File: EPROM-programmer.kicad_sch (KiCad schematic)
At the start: 83 parts, among them J1 ZIF-socket, J10 AMP_VPP, J2 ISP, J3 DAC_VCC, J4 DAC_VPP, J5 GND, J6 Barrel_Jack_Switch, J7 ZIF_VCC, J8 AMP_VCC, J9 GND, P1 USB-C, Q1 BC327, Q2 BC327, Q3 BC327, Q4 BC327, Q5 BC327, Q6 BC327, SW1 SW_Push, U1 ATmega1284-P, U2 MCP2221AxP, U3 MCP4812, U4 LM358, U5 ULN2003, U6 LM317_TO-220, U7 LM317_TO-220, Y1 20M

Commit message: Route VPP-stuff
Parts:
- removed R11, R21, R23: 5.1K, Resistor_THT:R_Axial_DIN0207_L6.3mm_D2.5mm_P10.16mm_Horizontal, symbol Device:R
- added RN1: 4K7, Resistor_THT:R_Array_SIP4, symbol Device:R_Network03_Split
- R12, R15, R22, R24: value 5.1K -> 5K1
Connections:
- net AMP_VPP: now also RN1.1 (R1), RN1.1 (R1), RN1.1 (R1)
- net at Q5.2 (B), R22.1: now also RN1.3 (R2.2)
- net at Q4.2 (B), R12.1: now also RN1.4 (R3.2)
- net at Q6.2 (B), R24.1: now also RN1.2 (R1.2)
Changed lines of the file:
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@@
 	)
 	(symbol
+		(lib_id "Device:R_Network03_Split")
+		(at 260.35 33.02 90)
+		(unit 3)
+		(exclude_from_sim no)
+		(in_bom yes)
+		(on_board yes)
+		(dnp no)
+		(fields_autoplaced yes)
+		(property "Reference" "RN1"
+			(at 260.35 26.67 90)
+			(effects
+				(font
+					(size 1.27 1.27)
+				)
+			)
+		)
+		(property "Value" "4K7"
+			(at 260.35 29.21 90)
+			(effects
+				(font
+					(size 1.27 1.27)
+				)
+			)
+		)
+		(property "Footprint" "Resistor_THT:R_Array_SIP4"
+			(at 260.35 35.052 90)
+			(effects
+				(font
+					(size 1.27 1.27)
+				)
+				(hide yes)
+			)
+		)
+		(property "Datasheet" "http://www.vishay.com/docs/31509/csc.pdf"
+			(at 260.35 33.02 0)
+			(effects
+				(font
+					(size 1.27 1.27)
+				)
+				(hide yes)
+			)
+		)
+		(property "Description" "3 resistor network, star topology, bussed resistors, split"
+			(at 260.35 33.02 0)
+			(effects
+				(font
+					(size 1.27 1.27)
+				)
+				(hide yes)
+			)
+		)
+		(pin "1"
+		)
+		(pin "3"
+		)
+		(pin "4"
+		)
+		(pin "2"
+		)
+		(instances
+			(project "EPROM-programmer"
+				(path "/8c5576b1-cb3e-4456-837b-2f47818a03ab"
+					(reference "RN1")
+					(unit 3)
+				)
+			)
+		)
+	)
+	(symbol
 		(lib_id "Device:C")
 		(at 92.71 161.29 0)
@@
 	)
 	(symbol
+		(lib_id "Device:R_Network03_Split")
+		(at 260.35 62.23 90)
+		(unit 2)
+		(exclude_from_sim no)
+		(in_bom yes)
+		(on_board yes)
+		(dnp no)
+		(fields_autoplaced yes)
+		(property "Reference" "RN1"
+			(at 260.35 55.88 90)
+			(effects
+				(font
+					(size 1.27 1.27)
+				)
+			)
+		)
+		(property "Value" "4K7"
+			(at 260.35 58.42 90)
+			(effects
+				(font
+					(size 1.27 1.27)
+				)
+			)
+		)
+		(property "Footprint" "Resistor_THT:R_Array_SIP4"
+			(at 260.35 64.262 90)
+			(effects
+				(font
+					(size 1.27 1.27)
+				)
+				(hide yes)
+			)
+		)
+		(property "Datasheet" "http://www.vishay.com/docs/31509/csc.pdf"
+			(at 260.35 62.23 0)
+			(effects
+				(font
+					(size 1.27 1.27)
+				)
+				(hide yes)
+			)
+		)
+		(property "Description" "3 resistor network, star topology, bussed resistors, split"
+			(at 260.35 62.23 0)
+			(effects
+				(font
+					(size 1.27 1.27)
+				)
+				(hide yes)
+			)
+		)
+		(pin "1"
+		)
+		(pin "3"
+		)
+		(pin "4"
+		)
+		(pin "2"
+		)
+		(instances
+			(project ""
+				(path "/8c5576b1-cb3e-4456-837b-2f47818a03ab"
+					(reference "RN1")
+					(unit 2)
+				)
+			)
+		)
+	)
+	(symbol
 		(lib_id "Device:R")
 		(at 259.08 129.54 0)
@@
 			)
 		)
-		(property "Value" "5.1K"
+		(property "Value" "5K1"
 			(at 270.51 71.12 0)
 			(effects
@@
 			)
 		)
-		(property "Value" "5.1K"
+		(property "Value" "5K1"
 			(at 270.51 100.33 0)
 			(effects
@@
 	)
 	(symbol
-		(lib_id "Device:R")
-		(at 260.35 91.44 90)
-		(unit 1)
-		(exclude_from_sim no)
-		(in_bom yes)
-		(on_board yes)
-		(dnp no)
-		(property "Reference" "R23"
-			(at 261.62 88.9 90)
-			(effects
-				(font
-					(size 1.27 1.27)
-				)
-				(justify left)
-			)
-		)
-		(property "Value" "5.1K"
-			(at 261.62 86.36 90)
-			(effects
-				(font
-					(size 1.27 1.27)
-				)
-				(justify left)
-			)
-		)
-		(property "Footprint" "Resistor_THT:R_Axial_DIN0207_L6.3mm_D2.5mm_P10.16mm_Horizontal"
-			(at 260.35 93.218 90)
-			(effects
-				(font
-					(size 1.27 1.27)
-				)
-				(hide yes)
-			)
-		)
-		(property "Datasheet" "~"
-			(at 260.35 91.44 0)
-			(effects
-				(font
-					(size 1.27 1.27)
-				)
-				(hide yes)
-			)
-		)
-		(property "Description" ""
-			(at 260.35 91.44 0)
-			(effects
-				(font
-					(size 1.27 1.27)
-				)
-				(hide yes)
-			)
-		)
-		(pin "1"
-		)
-		(pin "2"
-		)
-		(instances
-			(project "EPROM-programmer"
-				(path "/8c5576b1-cb3e-4456-837b-2f47818a03ab"
-					(reference "R23")
-					(unit 1)
-				)
-			)
-		)
-	)
-	(symbol
 		(lib_name "GND_1")
 		(lib_id "power:GND")
@@
 			)
 		)
-		(property "Value" "5.1K"
+		(property "Value" "5K1"
 			(at 171.45 49.53 0)
 			(effects
@@
 	)
 	(symbol
-		(lib_id "Device:R")
-		(at 260.35 33.02 90)
-		(unit 1)
-		(exclude_from_sim no)
-		(in_bom yes)
-		(on_board yes)
-		(dnp no)
-		(property "Reference" "R11"
-			(at 261.62 30.48 90)
-			(effects
-				(font
-					(size 1.27 1.27)
-				)
-				(justify left)
-			)
-		)
-		(property "Value" "5.1K"
-			(at 261.62 27.94 90)
-			(effects
-				(font
-					(size 1.27 1.27)
-				)
-				(justify left)
-			)
-		)
-		(property "Footprint" "Resistor_THT:R_Axial_DIN0207_L6.3mm_D2.5mm_P10.16mm_Horizontal"
-			(at 260.35 34.798 90)
-			(effects
-				(font
-					(size 1.27 1.27)
-				)
-				(hide yes)
-			)
-		)
-		(property "Datasheet" "~"
-			(at 260.35 33.02 0)
-			(effects
-				(font
-					(size 1.27 1.27)
-				)
-				(hide yes)
-			)
-		)
-		(property "Description" ""
-			(at 260.35 33.02 0)
-			(effects
-				(font
-					(size 1.27 1.27)
-				)
-				(hide yes)
-			)
-		)
-		(pin "1"
-		)
-		(pin "2"
-		)
-		(instances
-			(project "EPROM-programmer"
-				(path "/8c5576b1-cb3e-4456-837b-2f47818a03ab"
-					(reference "R11")
-					(unit 1)
-				)
-			)
-		)
-	)
-	(symbol
 		(lib_name "GND_1")
 		(lib_id "power:GND")
@@
 			)
 		)
-		(property "Value" "5.1K"
+		(property "Value" "5K1"
 			(at 270.51 41.91 0)
 			(effects
@@
 	)
 	(symbol
-		(lib_id "Device:R")
-		(at 260.35 62.23 90)
-		(unit 1)
-		(exclude_from_sim no)
-		(in_bom yes)
-		(on_board yes)
-		(dnp no)
-		(property "Reference" "R21"
-			(at 261.62 59.69 90)
-			(effects
-				(font
-					(size 1.27 1.27)
-				)
-				(justify left)
-			)
-		)
-		(property "Value" "5.1K"
-			(at 261.62 57.15 90)
-			(effects
-				(font
-					(size 1.27 1.27)
-				)
-				(justify left)
-			)
-		)
-		(property "Footprint" "Resistor_THT:R_Axial_DIN0207_L6.3mm_D2.5mm_P10.16mm_Horizontal"
-			(at 260.35 64.008 90)
-			(effects
-				(font
-					(size 1.27 1.27)
-				)
-				(hide yes)
-			)
-		)
-		(property "Datasheet" "~"
-			(at 260.35 62.23 0)
-			(effects
-				(font
-					(size 1.27 1.27)
-				)
-				(hide yes)
-			)
-		)
-		(property "Description" ""
-			(at 260.35 62.23 0)
-			(effects
-				(font
-					(size 1.27 1.27)
-				)
-				(hide yes)
-			)
-		)
-		(pin "1"
-		)
-		(pin "2"
-		)
-		(instances
-			(project "EPROM-programmer"
-				(path "/8c5576b1-cb3e-4456-837b-2f47818a03ab"
-					(reference "R21")
-					(unit 1)
-				)
-			)
-		)
-	)
-	(symbol
 		(lib_name "GND_1")
 		(lib_id "power:GND")
@@
 					(unit 1)
 				)
+			)
+		)
+	)
+	(symbol
+		(lib_id "Device:R_Network03_Split")
+		(at 260.35 91.44 90)
+		(unit 1)
+		(exclude_from_sim no)
+		(in_bom yes)
+		(on_board yes)
+		(dnp no)
+		(fields_autoplaced yes)
+		(property "Reference" "RN1"
+			(at 260.35 85.09 90)
+			(effects
+				(font
+					(size 1.27 1.27)
+				)
+			)
+		)
+		(property "Value" "4K7"
+			(at 260.35 87.63 90)
+			(effects
+				(font
+					(size 1.27 1.27)
+				)
+			)
+		)
+		(property "Footprint" "Resistor_THT:R_Array_SIP4"
+			(at 260.35 93.472 90)
+			(effects
+				(font
+					(size 1.27 1.27)
+				)
+				(hide yes)
+			)
+		)
+		(property "Datasheet" "http://www.vishay.com/docs/31509/csc.pdf"
+			(at 260.35 91.44 0)
+			(effects
+				(font
+					(size 1.27 1.27)
+				)
+				(hide yes)
+			)
+		)
+		(property "Description" "3 resistor network, star topology, bussed resistors, split"
+			(at 260.35 91.44 0)
+			(effects
+				(font
+					(size 1.27 1.27)
+				)
+				(hide yes)
+			)
+		)
+		(pin "1"
+		)
+		(pin "3"
+		)
+		(pin "4"
+		)
+		(pin "2"
+		)
+		(instances
+			(project "EPROM-programmer"
+				(path "/8c5576b1-cb3e-4456-837b-2f47818a03ab"
+					(reference "RN1")
+					(unit 1)
+				)

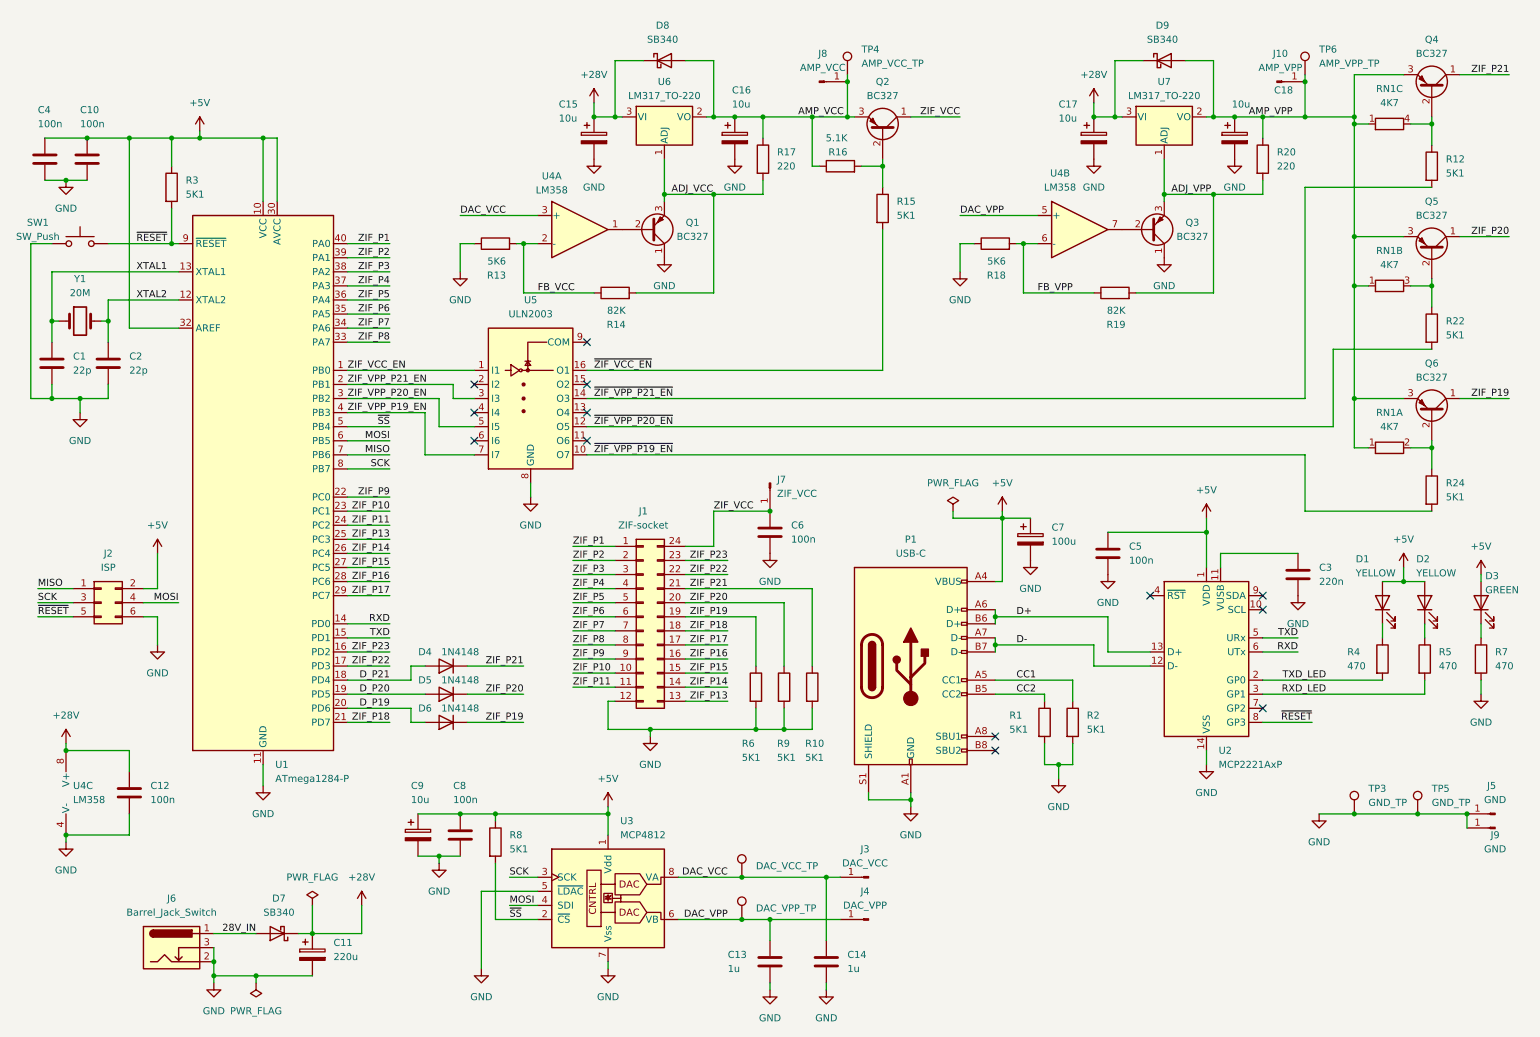
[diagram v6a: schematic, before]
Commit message: Add switching supply for VCC to ZIF-socket
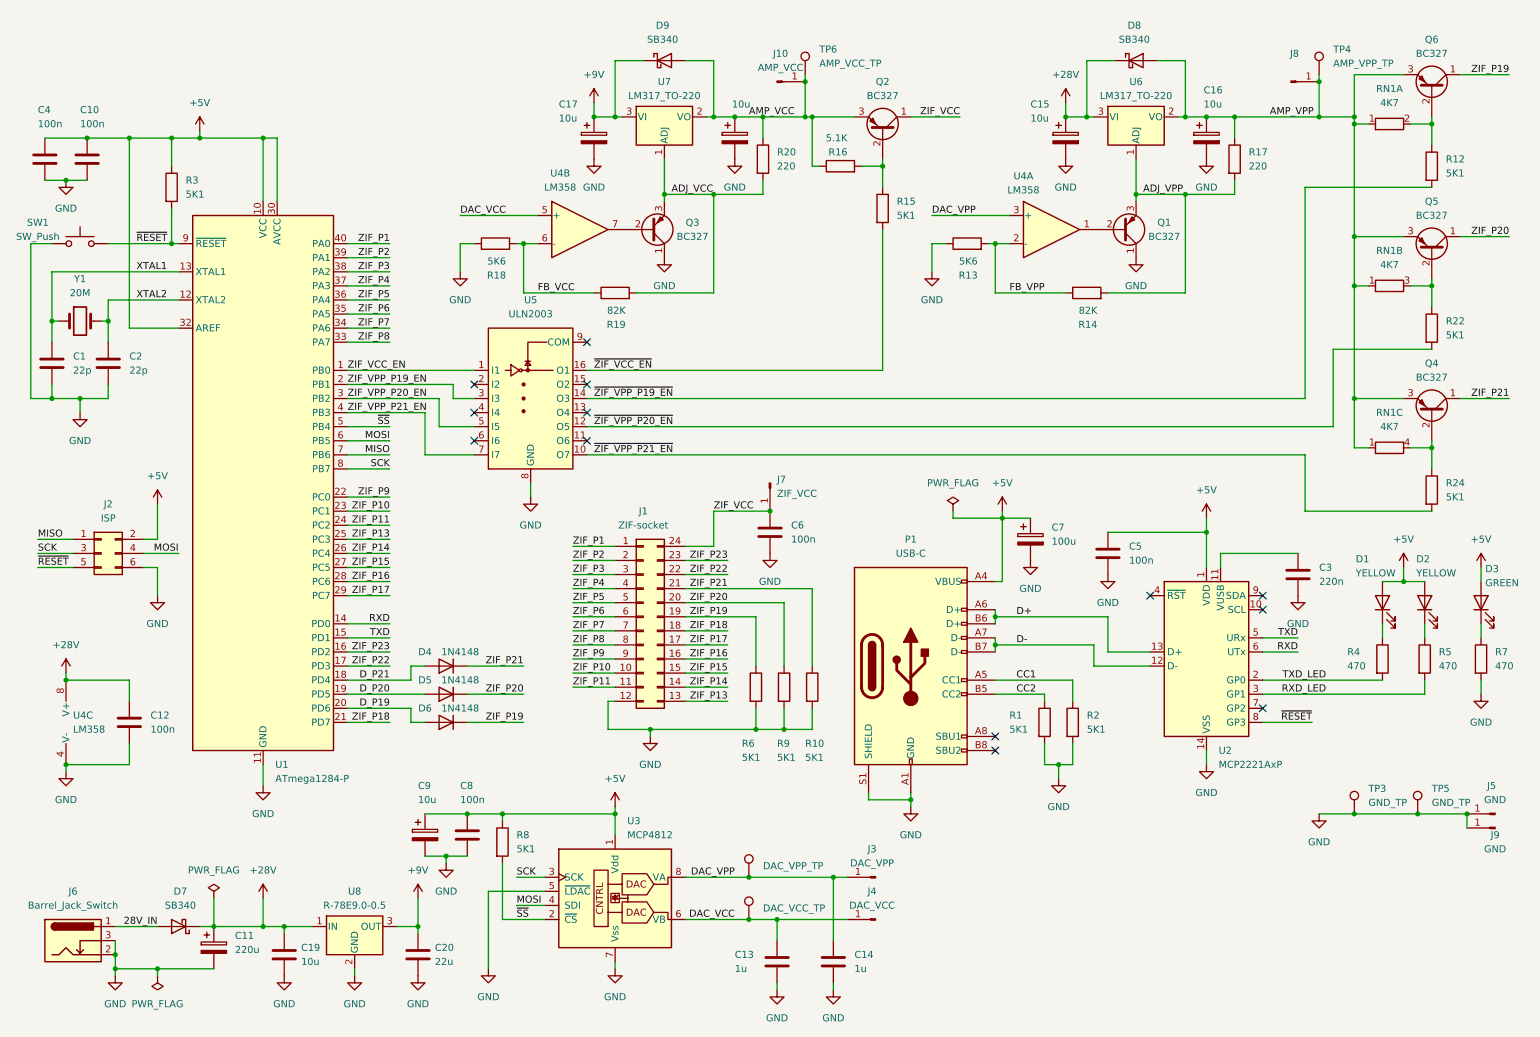
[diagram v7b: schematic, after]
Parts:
- added C19: 10u, Capacitor_THT:C_Rect_L7.0mm_W4.5mm_P5.00mm, symbol Device:C
- added C20: 22u, Capacitor_THT:C_Rect_L7.0mm_W4.5mm_P5.00mm, symbol Device:C
- added U8: R-78E9.0-0.5, Converter_DCDC:Converter_DCDC_RECOM_R-78E-0.5_THT, symbol Regulator_Switching:R-78E9.0-0.5
- J10: value AMP_VPP -> AMP_VCC
- J3: value DAC_VCC -> DAC_VPP
- J4: value DAC_VPP -> DAC_VCC
- J8: value AMP_VCC -> AMP_VPP
- TP1: value DAC_VCC_TP -> DAC_VPP_TP
- TP2: value DAC_VPP_TP -> DAC_VCC_TP
- TP4: value AMP_VCC_TP -> AMP_VPP_TP
- TP6: value AMP_VPP_TP -> AMP_VCC_TP
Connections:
- net +28V: now also C19.1, U8.1 (IN); no longer C17.1, D9.1 (K), U7.3 (VI)
- net ADJ_VCC: now also Q3.3 (E), R19.2, R20.2, U7.1 (ADJ); no longer Q1.3 (E), R14.2, R17.2, U6.1 (ADJ)
- net ADJ_VPP: now also Q1.3 (E), R14.2, R17.2, U6.1 (ADJ); no longer Q3.3 (E), R19.2, R20.2, U7.1 (ADJ)
- net AMP_VCC: now also C18.1, D9.2 (A), J10.1 (Pin_1), R20.1, TP6.1, U7.2 (VO); no longer C16.1, D8.2 (A), J8.1 (Pin_1), R17.1, TP4.1, U6.2 (VO)
- net AMP_VPP: now also C16.1, D8.2 (A), J8.1 (Pin_1), R17.1, TP4.1, U6.2 (VO); no longer C18.1, D9.2 (A), J10.1 (Pin_1), R20.1, TP6.1, U7.2 (VO)
- net DAC_VCC: now also C13.1, J4.1 (Pin_1), TP2.1, U3.6 (VB), U4.5 (+); no longer C14.1, J3.1 (Pin_1), TP1.1, U3.8 (VA), U4.3 (+)
- net DAC_VPP: now also C14.1, J3.1 (Pin_1), TP1.1, U3.8 (VA), U4.3 (+); no longer C13.1, J4.1 (Pin_1), TP2.1, U3.6 (VB), U4.5 (+)
- net FB_VCC: now also R18.2, R19.1, U4.6 (-); no longer R13.2, R14.1, U4.2 (-)
- net FB_VPP: now also R13.2, R14.1, U4.2 (-); no longer R18.2, R19.1, U4.6 (-)
- net GND: now also C19.2, C20.2, U8.2 (GND)
- net ZIF_VPP_P19_EN: now also U1.2 (PB1), U5.3 (I3); no longer U1.4 (PB3), U5.7 (I7)
- net ZIF_VPP_P21_EN: now also U1.4 (PB3), U5.7 (I7); no longer U1.2 (PB1), U5.3 (I3)
- net ~{ZIF_VPP_P19_EN}: now also R12.2, U5.14 (O3); no longer R24.2, U5.10 (O7)
- net ~{ZIF_VPP_P21_EN}: now also R24.2, U5.10 (O7); no longer R12.2, U5.14 (O3)
- net at Q4.2 (B), RN1.4 (R3.2): now also R24.1; no longer R12.1
- net at Q6.2 (B), RN1.2 (R1.2): now also R12.1; no longer R24.1
- new net +9V: C17.1, C20.1, D9.1 (K), U7.3 (VI), U8.3 (OUT)
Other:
- moved on the sheet: C11, C12, C13, C14, C15, C16, C17, C8, C9, D7, D8, D9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

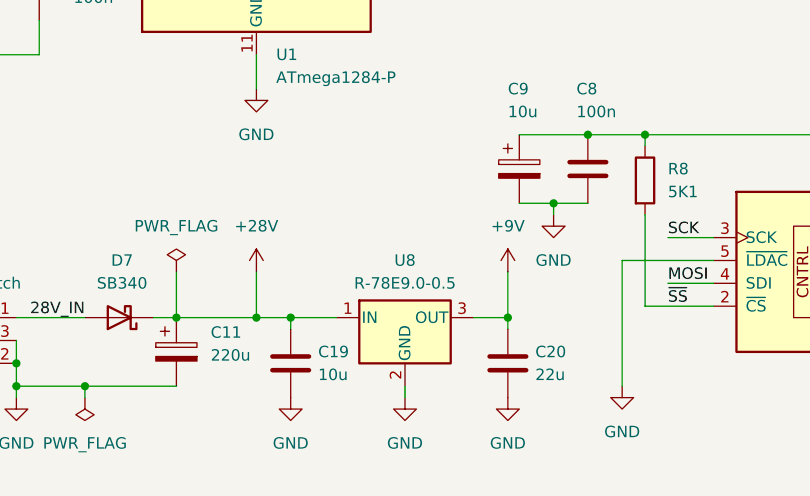
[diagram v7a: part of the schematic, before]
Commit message: Use R-78K9.0-0.5 instead of R-78E9.0-0.5
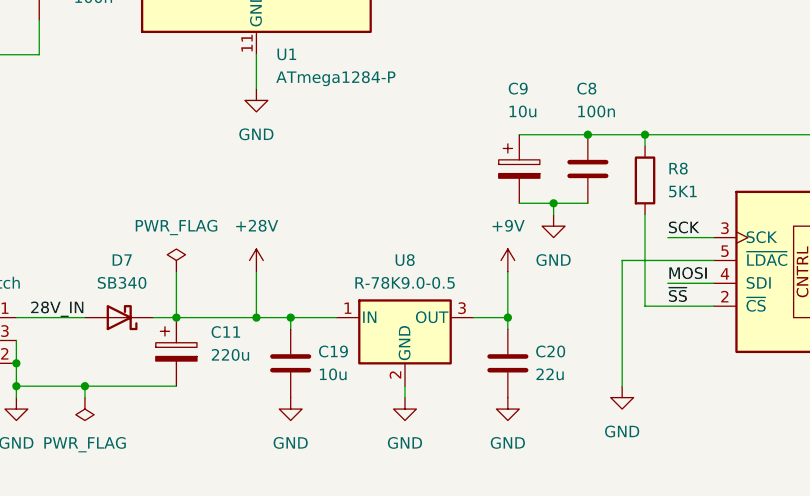
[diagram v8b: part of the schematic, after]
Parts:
- U8: value R-78E9.0-0.5 -> R-78K9.0-0.5
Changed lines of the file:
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@@
 			)
 		)
-		(property "Value" "R-78E9.0-0.5"
+		(property "Value" "R-78K9.0-0.5"
 			(at 73.66 173.99 0)
 			(effects
@@
 			)
 		)
-		(property "Datasheet" "https://www.recom-power.com/pdf/Innoline/R-78Exx-0.5.pdf"
+		(property "Datasheet" "https://www.recom-power.com/pdf/Innoline/R-78K-0.5.pdf"
 			(at 73.66 177.8 0)
 			(effects
@@
 			)
 		)
-		(property "Description" "500mA Step-Down DC/DC-Regulator, 12-28V input, 9V fixed Output Voltage, LM78xx replacement, -40°C to +85°C, SIP3"
+		(property "Description" "500mA Step-Down DC/DC-Regulator, 12-36V input, 9V fixed Output Voltage, LM78xx replacement, -40°C to +90°C, SIP3"
 			(at 73.66 177.8 0)
 			(effects
